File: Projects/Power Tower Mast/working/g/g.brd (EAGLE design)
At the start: 16.5 x 21.6 mm, 42 parts

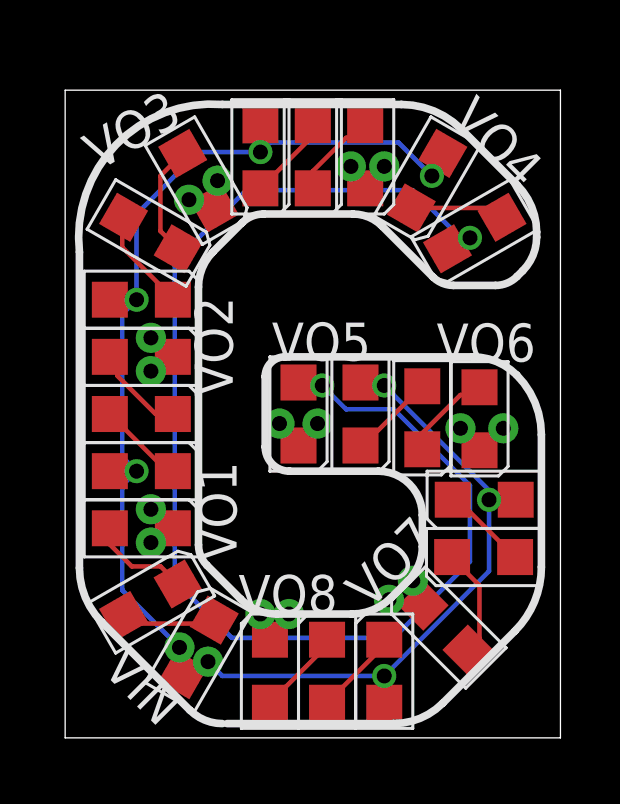
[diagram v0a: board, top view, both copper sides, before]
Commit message: deleted f from working; updated g
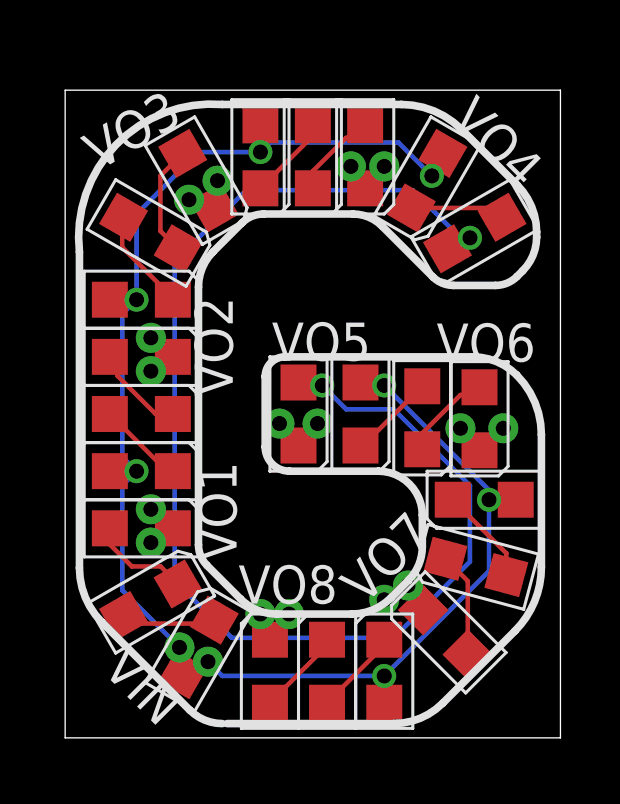
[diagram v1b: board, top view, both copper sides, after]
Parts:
- moved LED20 0.42 mm to (13.7, 5.70), turned to 75 degrees
- moved VO7 0.22 mm to (11.4, 5.08)
- moved LED21 0.16 mm to (12.7, 3.52)
- moved VO15 0.16 mm to (10.6, 4.60)
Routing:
- net N$28: track 2.87 -> 3.42 mm
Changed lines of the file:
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@@
 <attribute name="VALUE" x="7.62" y="12.85875" size="1.016" layer="27" ratio="15" rot="R270"/>
 </element>
-<element name="LED21" library="CyberRailGuru" package="LED_0805" value="" x="12.67816875" y="3.675915625" smashed="yes" rot="R45">
-<attribute name="VALUE" x="15.709" y="3.788171875" size="1.016" layer="27" ratio="15" rot="R135"/>
-</element>
-<element name="LED20" library="CyberRailGuru" package="LED_0805" value="" x="13.94873125" y="6.0268" smashed="yes" rot="R90">
-<attribute name="VALUE" x="16.01248125" y="8.2493" size="1.016" layer="27" ratio="15" rot="R180"/>
+<element name="LED21" library="CyberRailGuru" package="LED_0805" value="" x="12.67816875" y="3.517165625" smashed="yes" rot="R45">
+<attribute name="VALUE" x="15.709" y="3.629421875" size="1.016" layer="27" ratio="15" rot="R135"/>
+</element>
+<element name="LED20" library="CyberRailGuru" package="LED_0805" value="" x="13.691603125" y="5.698378125" smashed="yes" rot="R75">
+<attribute name="VALUE" x="16.260259375" y="7.311009375" size="1.016" layer="27" ratio="15" rot="R165"/>
 </element>
 <element name="LED19" library="CyberRailGuru" package="LED_0805" value="" x="13.97" y="7.9375" smashed="yes" rot="R90">
@@
 <attribute name="VALUE" x="11.65225" y="8.28675" size="1.27" layer="27" ratio="10"/>
 </element>
-<element name="VO7" library="CyberRailGuru" package="P1-20" value="" x="11.58875" y="5.23875" smashed="yes">
-<attribute name="NAME" x="10.135953125" y="4.241346875" size="1.27" layer="25" ratio="15" rot="R45"/>
-<attribute name="VALUE" x="10.06475" y="3.20675" size="1.27" layer="27" ratio="10"/>
+<element name="VO7" library="CyberRailGuru" package="P1-20" value="" x="11.43" y="5.08" smashed="yes">
+<attribute name="NAME" x="9.977203125" y="4.400096875" size="1.27" layer="25" ratio="15" rot="R45"/>
+<attribute name="VALUE" x="9.906" y="3.048" size="1.27" layer="27" ratio="10"/>
 </element>
 <element name="VIN1" library="CyberRailGuru" package="P1-20" value="" x="4.7625" y="2.54" smashed="yes">
@@
 <attribute name="VALUE" x="13.081" y="8.28675" size="1.27" layer="27" ratio="10"/>
 </element>
-<element name="VO15" library="CyberRailGuru" package="P1-20" value="" x="10.795" y="4.60375" smashed="yes">
-<attribute name="VALUE" x="9.271" y="2.57175" size="1.27" layer="27" ratio="10"/>
+<element name="VO15" library="CyberRailGuru" package="P1-20" value="" x="10.63625" y="4.60375" smashed="yes">
+<attribute name="VALUE" x="9.11225" y="2.57175" size="1.27" layer="27" ratio="10"/>
 </element>
 <element name="LED22" library="CyberRailGuru" package="LED_0805" value="" x="10.63625" y="2.2225" smashed="yes">
@@
 </element>
 <element name="VO8" library="CyberRailGuru" package="P1-20" value="" x="7.46125" y="4.1275" smashed="yes">
-<attribute name="NAME" x="5.7785" y="4.15925" size="1.27" layer="25" ratio="15"/>
+<attribute name="NAME" x="5.7785" y="4.47675" size="1.27" layer="25" ratio="15"/>
 <attribute name="VALUE" x="5.93725" y="2.0955" size="1.27" layer="27" ratio="10"/>
 </element>
@@
 <contactref element="LED21" pad="A"/>
 <contactref element="LED20" pad="C"/>
-<wire x1="12.89873125" y1="6.0268" x2="12.89873125" y2="5.99251875" width="0.1524" layer="1"/>
-<wire x1="12.89873125" y1="5.99251875" x2="13.81125" y2="5.08" width="0.1524" layer="1"/>
-<wire x1="13.81125" y1="5.08" x2="13.81125" y2="3.324075" width="0.1524" layer="1"/>
-<wire x1="13.81125" y1="3.324075" x2="13.420628125" y2="2.933453125" width="0.1524" layer="1"/>
+<wire x1="13.420628125" y1="2.774703125" x2="13.420628125" y2="5.2268875" width="0.1524" layer="1"/>
+<wire x1="13.420628125" y1="5.2268875" x2="12.677378125" y2="5.9701375" width="0.1524" layer="1"/>
 </signal>
 <signal name="N$28">
@@
 <contactref element="LED19" pad="C"/>
 <wire x1="12.92" y1="7.9375" x2="13.08803125" y2="7.9375" width="0.1524" layer="1"/>
-<wire x1="13.08803125" y1="7.9375" x2="14.99873125" y2="6.0268" width="0.1524" layer="1"/>
+<wire x1="14.705825" y1="5.426615625" x2="14.705825" y2="6.151675" width="0.1524" layer="1"/>
+<wire x1="14.705825" y1="6.151675" x2="12.92" y2="7.9375" width="0.1524" layer="1"/>
 </signal>
 <signal name="VOUT7">
@@
 <contactref element="VO7" pad="TP"/>
 <contactref element="VO15" pad="TP"/>
-<wire x1="11.93570625" y1="4.418375" x2="11.93570625" y2="4.89179375" width="0.1524" layer="1"/>
-<wire x1="11.93570625" y1="4.89179375" x2="11.58875" y2="5.23875" width="0.1524" layer="1"/>
-<wire x1="11.58875" y1="5.23875" x2="11.43" y2="5.23875" width="0.1524" layer="1"/>
-<wire x1="11.43" y1="5.23875" x2="10.795" y2="4.60375" width="0.1524" layer="1"/>
+<wire x1="11.93570625" y1="4.259625" x2="11.93570625" y2="4.57429375" width="0.1524" layer="1"/>
+<wire x1="11.93570625" y1="4.57429375" x2="11.43" y2="5.08" width="0.1524" layer="1"/>
+<wire x1="11.43" y1="5.08" x2="11.1125" y2="5.08" width="0.1524" layer="1"/>
+<wire x1="11.1125" y1="5.08" x2="10.63625" y2="4.60375" width="0.1524" layer="1"/>
 </signal>
 <signal name="VIN">
